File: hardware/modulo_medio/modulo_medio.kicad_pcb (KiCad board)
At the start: 2 copper layers, 100 x 86 mm, 41 parts, among them J1 Backplane (IDC 2x8), J2 Entradas 0-7, J3 Entradas 8-15, J4 LEDs 0-7, J5 LEDs 8-15, J6 Analógico (joystick, acelerad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, SW1 Etiqueta (DIP 8 vias), U1 74HC165, U2 74HC165, U3 74HC165, U4 74HC595, U5 74HC595

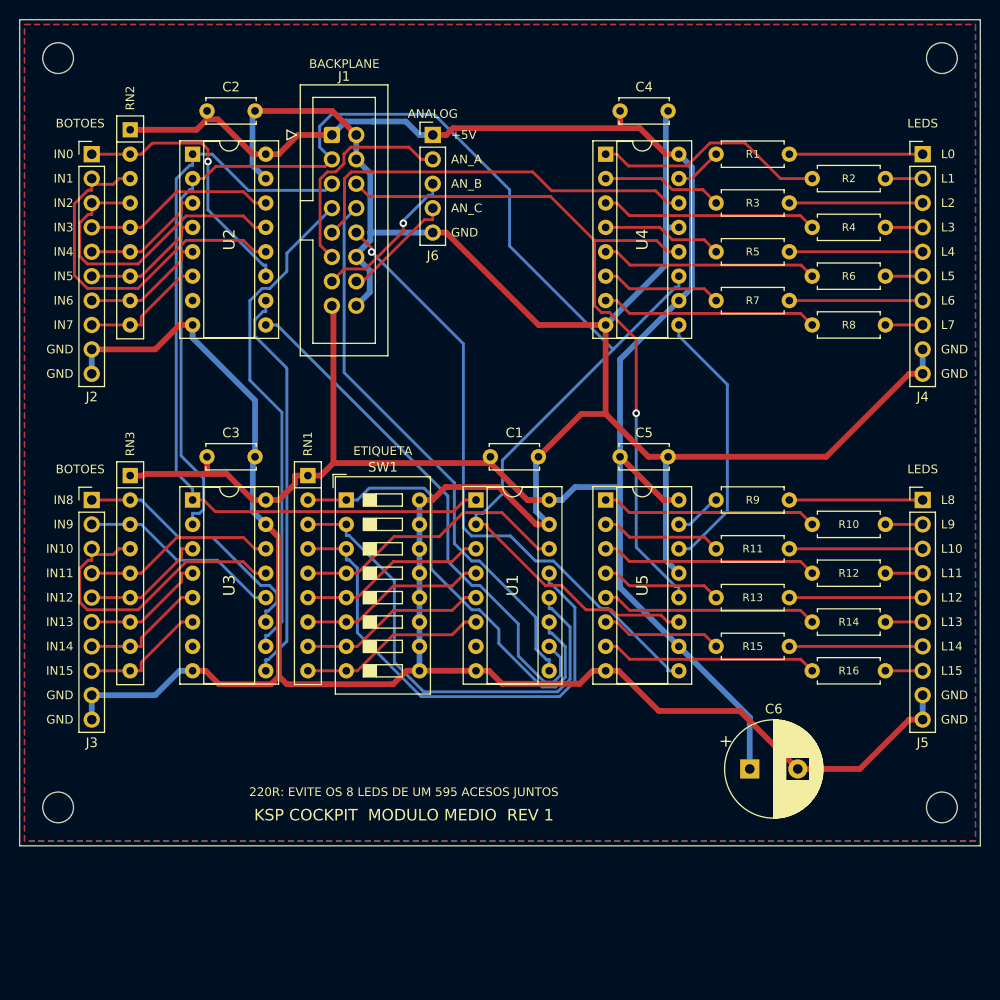
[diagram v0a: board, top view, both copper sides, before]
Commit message: Módulo médio: 3 × 74HC595 e 12 jacks JST-XH para os korry (#45)
- Esquema: U6 (74HC595) no fim da cadeia de saída, com R17–R24 (220 Ω)
  e C7; as barras J2–J5 viram 12 jacks JST-XH de 4 vias (K1 a K12:
  GND, IN(k-1), LED(2k-2), LED(2k-1)) e uma barra J2 com IN12–IN15.
- PCB refeita em 100 × 100 mm: K1–K6 na borda de cima, K7–K12 na de
  baixo; DRC sem erros e sem ligações faltando; Gerbers novos.
- Documentação: tabelas do módulo médio, ordem dos bytes (3 de saída),
  lista de peças e a ficha do korry com os jacks.


Claude-Session: https://claude.ai/code/session_01GYbCKeH4xeEesJ5HC66wNT

Co-authored-by: Claude <noreply@anthropic.com>
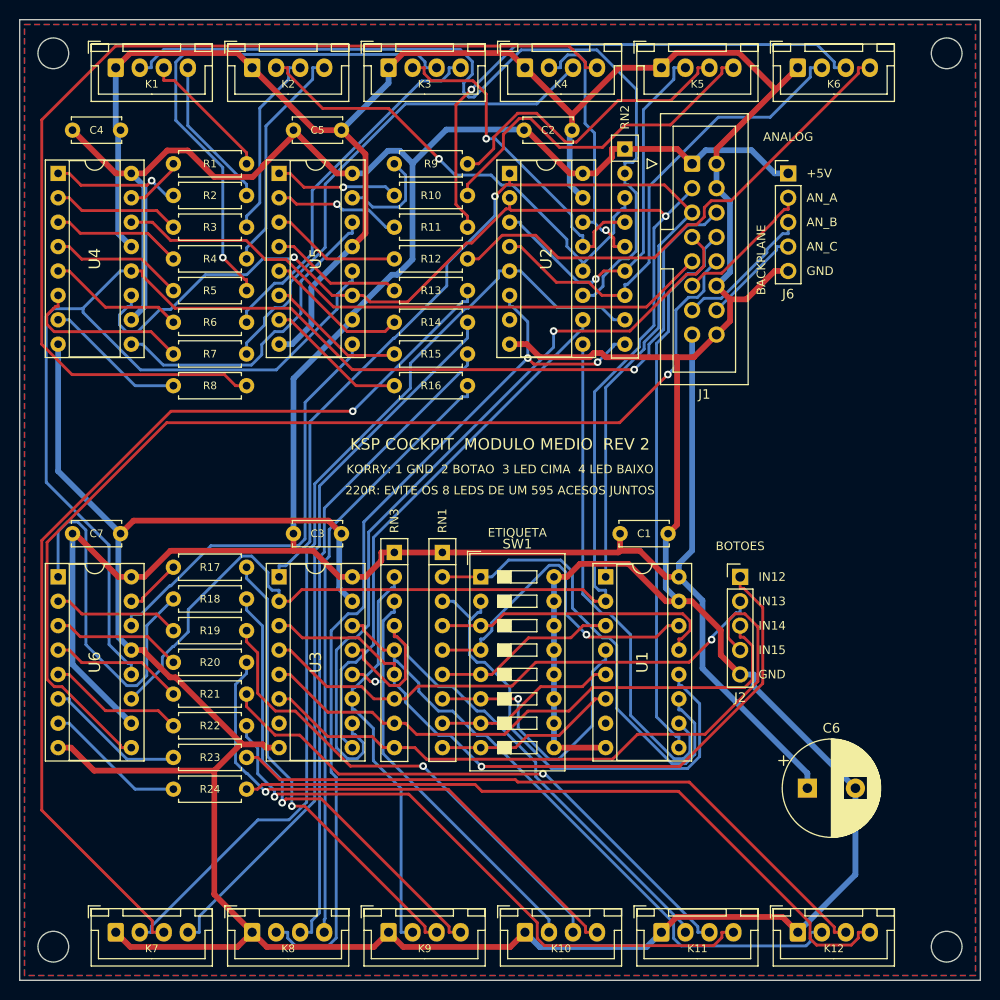
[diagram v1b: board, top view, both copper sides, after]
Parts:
- removed J3: Entradas 8-15, Connector_PinHeader_2.54mm:PinHeader_1x10_P2.54mm_Vertical
- removed J4: LEDs 0-7, Connector_PinHeader_2.54mm:PinHeader_1x10_P2.54mm_Vertical
- removed J5: LEDs 8-15, Connector_PinHeader_2.54mm:PinHeader_1x10_P2.54mm_Vertical
- added C7: 100nF, Capacitor_THT:C_Disc_D5.0mm_W2.5mm_P5.00mm, F.Cu at (5.50, 53.5)
- added K1: Korry 1, Connector_JST:JST_XH_B4B-XH-A_1x04_P2.50mm_Vertical, F.Cu at (10.0, 5.00)
- added K10: Korry 10, Connector_JST:JST_XH_B4B-XH-A_1x04_P2.50mm_Vertical, F.Cu at (52.6, 95.0)
- added K11: Korry 11, Connector_JST:JST_XH_B4B-XH-A_1x04_P2.50mm_Vertical, F.Cu at (66.8, 95.0)
- added K12: Korry 12, Connector_JST:JST_XH_B4B-XH-A_1x04_P2.50mm_Vertical, F.Cu at (81.0, 95.0)
- added K2: Korry 2, Connector_JST:JST_XH_B4B-XH-A_1x04_P2.50mm_Vertical, F.Cu at (24.2, 5.00)
- added K3: Korry 3, Connector_JST:JST_XH_B4B-XH-A_1x04_P2.50mm_Vertical, F.Cu at (38.4, 5.00)
- added K4: Korry 4, Connector_JST:JST_XH_B4B-XH-A_1x04_P2.50mm_Vertical, F.Cu at (52.6, 5.00)
- added K5: Korry 5, Connector_JST:JST_XH_B4B-XH-A_1x04_P2.50mm_Vertical, F.Cu at (66.8, 5.00)
- added K6: Korry 6, Connector_JST:JST_XH_B4B-XH-A_1x04_P2.50mm_Vertical, F.Cu at (81.0, 5.00)
- added K7: Korry 7, Connector_JST:JST_XH_B4B-XH-A_1x04_P2.50mm_Vertical, F.Cu at (10.0, 95.0)
- added K8: Korry 8, Connector_JST:JST_XH_B4B-XH-A_1x04_P2.50mm_Vertical, F.Cu at (24.2, 95.0)
- added K9: Korry 9, Connector_JST:JST_XH_B4B-XH-A_1x04_P2.50mm_Vertical, F.Cu at (38.4, 95.0)
- added R17: 220, Resistor_THT:R_Axial_DIN0207_L6.3mm_D2.5mm_P7.62mm_Horizontal, F.Cu at (16.0, 57.0)
- added R18: 220, Resistor_THT:R_Axial_DIN0207_L6.3mm_D2.5mm_P7.62mm_Horizontal, F.Cu at (16.0, 60.3)
- added R19: 220, Resistor_THT:R_Axial_DIN0207_L6.3mm_D2.5mm_P7.62mm_Horizontal, F.Cu at (16.0, 63.6)
- added R20: 220, Resistor_THT:R_Axial_DIN0207_L6.3mm_D2.5mm_P7.62mm_Horizontal, F.Cu at (16.0, 66.9)
- added R21: 220, Resistor_THT:R_Axial_DIN0207_L6.3mm_D2.5mm_P7.62mm_Horizontal, F.Cu at (16.0, 70.2)
- added R22: 220, Resistor_THT:R_Axial_DIN0207_L6.3mm_D2.5mm_P7.62mm_Horizontal, F.Cu at (16.0, 73.5)
- added R23: 220, Resistor_THT:R_Axial_DIN0207_L6.3mm_D2.5mm_P7.62mm_Horizontal, F.Cu at (16.0, 76.8)
- added R24: 220, Resistor_THT:R_Axial_DIN0207_L6.3mm_D2.5mm_P7.62mm_Horizontal, F.Cu at (16.0, 80.1)
- added U6: 74HC595, Package_DIP:DIP-16_W7.62mm_Socket, F.Cu at (4.00, 58.0)
- J2: value Entradas 0-7 -> Entradas 12-15; footprint Connector_PinHeader_2.54mm:PinHeader_1x10_P2.54mm_Vertical -> Connector_PinHeader_2.54mm:PinHeader_1x05_P2.54mm_Vertical
- moved J2 80.6 mm to (75.0, 58.0)
- moved R8 66.8 mm to (16.0, 38.1)
- moved R6 66.7 mm to (16.0, 31.5)
- moved R4 66.6 mm to (16.0, 24.9)
- moved R2 66.5 mm to (16.0, 18.3)
- moved C4 57.0 mm to (5.50, 11.5)
- moved U4 57.0 mm to (4.00, 16.0)
- moved R7 56.8 mm to (16.0, 34.8)
- moved R5 56.6 mm to (16.0, 28.2)
- moved R3 56.6 mm to (16.0, 21.6)
- moved R1 56.5 mm to (16.0, 15.0)
- moved R10 55.4 mm to (39.0, 18.3)
- moved R12 54.4 mm to (39.0, 24.9)
- moved R14 53.5 mm to (39.0, 31.5)
- moved R16 52.7 mm to (39.0, 38.1)
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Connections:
- J2 pad 1: /IN0 -> /IN12
- J2 pad 2: /IN1 -> /IN13
- J2 pad 3: /IN2 -> /IN14
- J2 pad 4: /IN3 -> /IN15
- J2 pad 5: /IN4 -> GND
- U5 pad 9: /SOUT595 -> /CH595_2
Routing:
- net GND: track 363.8 -> 519.6 mm
- net /LED7: track 3.88 -> 108.7 mm
- net /IN6: track 13.1 -> 102.3 mm
- net /LED12: track 13.9 -> 102.5 mm, vias 0 -> 1
- net /RCLK: track 78.0 -> 166.5 mm
- net /IN7: track 13.1 -> 95.9 mm, vias 0 -> 2
- net +5V: track 221.7 -> 300.8 mm
- net /LED23: track 0.00 -> 73.9 mm
- net /LED13: track 3.88 -> 76.3 mm
- net /LED22: track 0.00 -> 70.2 mm
- net /LED21: track 0.00 -> 64.9 mm, vias 0 -> 1
- net /IN12: track 13.1 -> 74.2 mm, vias 0 -> 1
- net /LED20: track 0.00 -> 59.6 mm, vias 0 -> 1
- net /IN0: track 28.7 -> 88.3 mm, vias 1 -> 0
- net /LED15: track 3.88 -> 63.4 mm
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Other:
- board size 100 x 86 mm -> 100 x 100 mm
- board text added: "KORRY: 1 GND 2 BOTAO 3 LED CIMA 4 LED BAIXO"
- board text added: "KSP COCKPIT MODULO MEDIO REV 2"
- board text removed: "IN0"
- board text removed: "IN1"
- board text removed: "IN10"
- board text removed: "IN11"
- board text removed: "IN2"
- board text removed: "IN3"
- board text removed: "IN4"
- board text removed: "IN5"
- board text removed: "IN6"
- board text removed: "IN7"
- board text removed: "IN8"
- board text removed: "IN9"
- board text removed: "KSP COCKPIT MODULO MEDIO REV 1"
- board text removed: "L0"
- board text removed: "L1"
- board text removed: "L10"
- board text removed: "L11"
- board text removed: "L12"
- board text removed: "L13"
- board text removed: "L14"
- board text removed: "L15"
- board text removed: "L2"
- board text removed: "L3"
- board text removed: "L4"
- board text removed: "L5"
- board text removed: "L6"
- board text removed: "L7"
- board text removed: "L8"
- board text removed: "L9"
- board text removed: "LEDS"
